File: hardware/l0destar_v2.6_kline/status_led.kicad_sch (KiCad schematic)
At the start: 6 parts

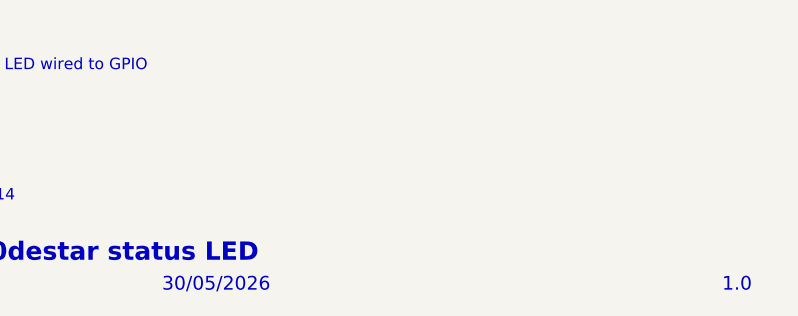
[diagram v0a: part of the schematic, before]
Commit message: fix sheet annotations
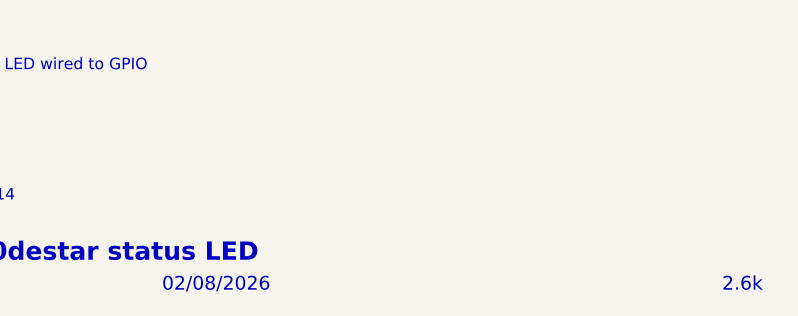
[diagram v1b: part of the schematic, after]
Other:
- note added: "02/08/2026"
- note added: "2.6k"
- note removed: "1.0"
- note removed: "30/05/2026"
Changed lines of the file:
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@@
 	(generator_version "10.0")
 	(paper "A4")
-	(text "1.0"
+	(text "2.6k"
 		(exclude_from_sim no)
 		(at 268.478 193.294 0)
@@
 		)
 	)
-	(text "30/05/2026"
+	(text "02/08/2026"
 		(exclude_from_sim no)
 		(at 206.248 193.294 0)
